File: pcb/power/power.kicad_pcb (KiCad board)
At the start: 2 copper layers, 50 x 40 mm, 98 parts, among them CON1 BARREL_JACK, P1 CONN_01X04, P2 CONN_01X04, P3 CONN_01X04, P4 USB_A, P5 CONN_01X03, P6 CONN_01X03, Q1 MMBT3904, Q2 MMBT3904, Q3 MMBT3904, Q4 MMBT3904, Q5 MMBT3904, Q6 MMBT3904, Q7 DMG2305UX, Q8 DMG2305UX, Q9 DMG2305UX, U1 LM2840, U2 TS30012, U3 LM324QT

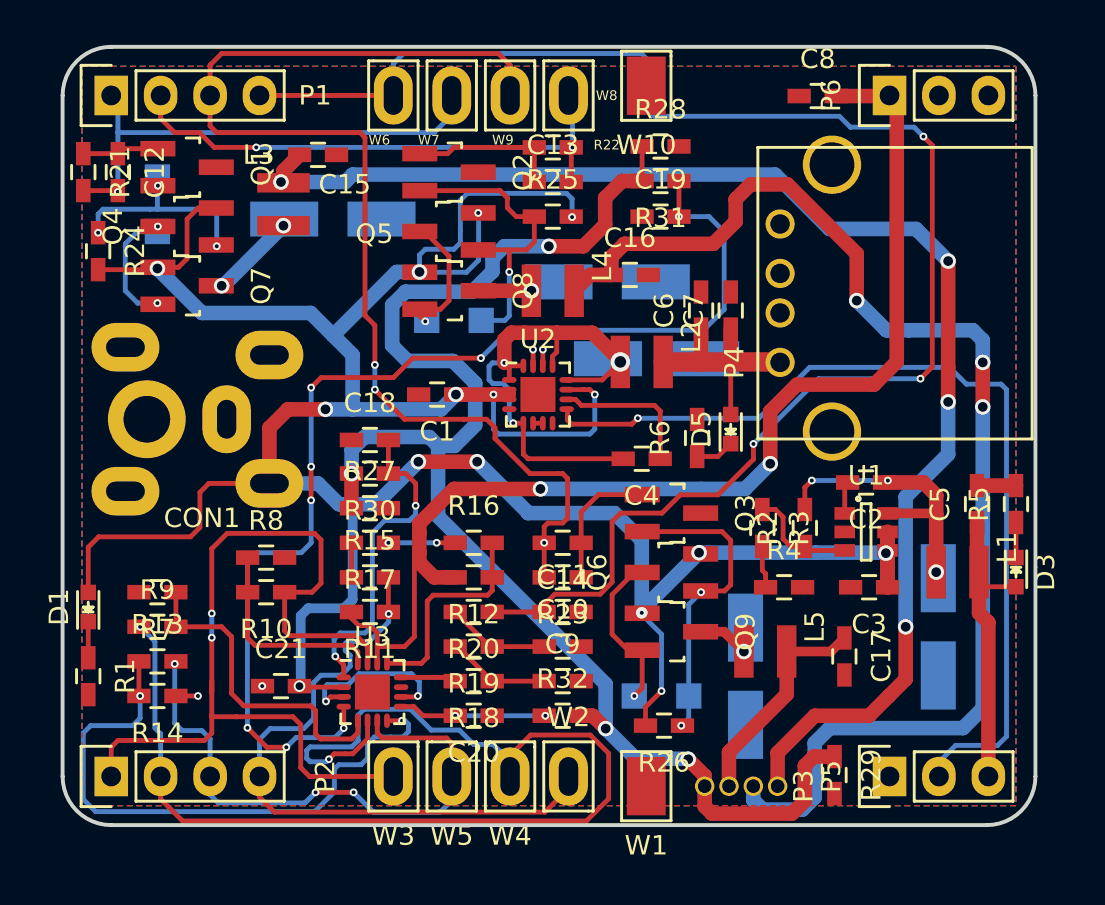
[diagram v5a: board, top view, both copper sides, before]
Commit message: Finished the layout. Could be produced like that. Some fine tuning will maybe be done if I see something, which bothers me.
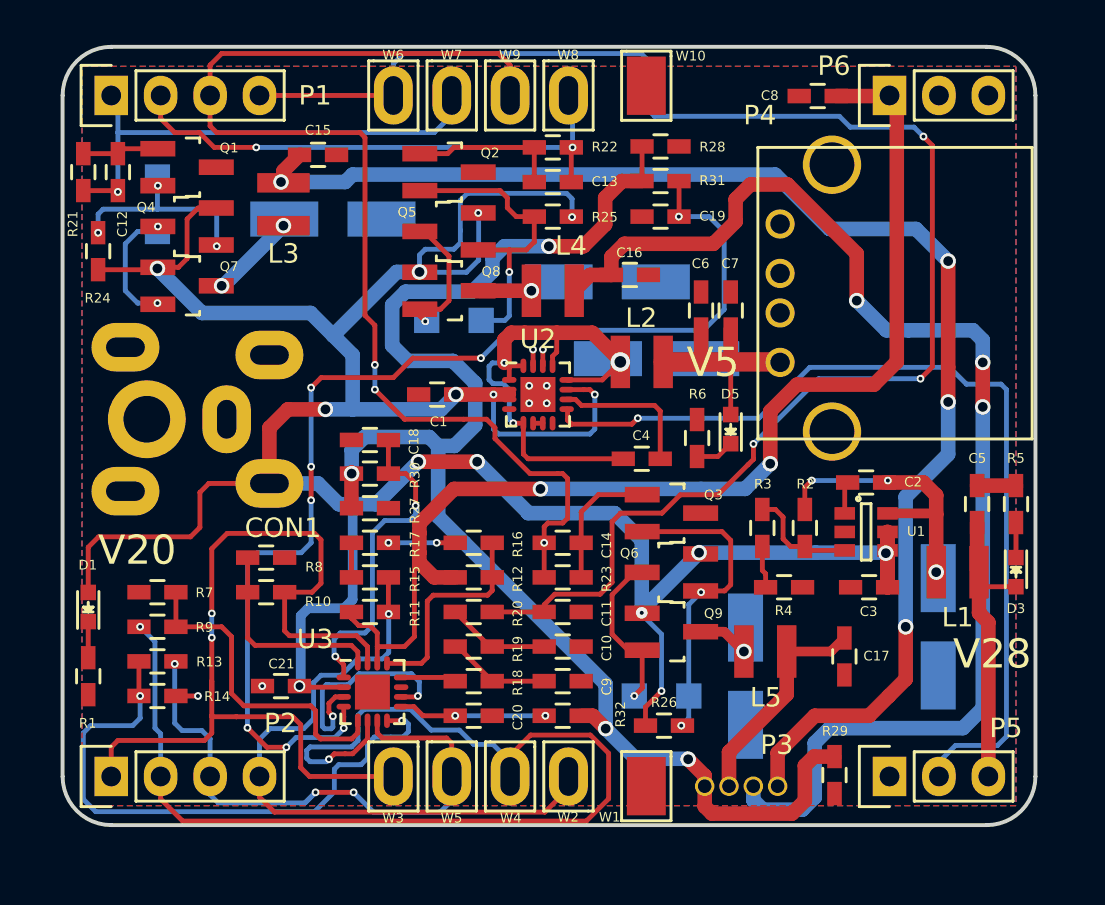
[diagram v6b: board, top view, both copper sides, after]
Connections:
- U2 pad 17: (no net) -> GND
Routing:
- net Net-(U3-Pad10): track 8.74 -> 11.9 mm
- net GND: track 8.54 -> 8.83 mm, vias 6 -> 10
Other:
- board text added: "V20"
- board text added: "V28"
- board text added: "V5"

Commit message: Fnished board. Producing output now.
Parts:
- added G***: LOGO, Additional:UU, B.Cu at (153.9, 110.4)
- added REF**: Via_GND_04, Additional:Via_GND_04, F.Cu at (156.9, 92.8)
- added REF**: Via_GND_04, Additional:Via_GND_04, F.Cu at (153.4, 116.8)
- added REF**: Via_GND_04, Additional:Via_GND_04, F.Cu at (153.4, 115.0)
- added REF**: Via_GND_04, Additional:Via_GND_04, F.Cu at (149.9, 114.9)
- added REF**: Via_GND_04, Additional:Via_GND_04, F.Cu at (153.4, 111.5)
- added REF**: Via_GND_04, Additional:Via_GND_04, F.Cu at (150.9, 90.8)
- added REF**: Via_GND_04, Additional:Via_GND_04, F.Cu at (151.9, 90.8)
- added REF**: Via_GND_04, Additional:Via_GND_04, F.Cu at (146.5, 90.8)
- added REF**: Via_GND_04, Additional:Via_GND_04, F.Cu at (154.5, 105.5)
- added REF**: Via_GND_04, Additional:Via_GND_04, F.Cu at (156.7, 105.5)
- added REF**: Via_GND_04, Additional:Via_GND_04, F.Cu at (158.7, 105.2)
- added REF**: Via_GND_04, Additional:Via_GND_04, F.Cu at (143.2, 116.6)
- added REF**: Via_GND_04, Additional:Via_GND_04, F.Cu at (161.6, 105.2)
- added REF**: Via_GND_04, Additional:Via_GND_04, F.Cu at (144.0, 91.1)
- added REF**: Via_GND_04, Additional:Via_GND_04, F.Cu at (149.6, 111.0)
- added REF**: Via_GND_04, Additional:Via_GND_04, F.Cu at (152.8, 94.3)
- added REF**: Via_GND_1, Additional:Via_GND_1, F.Cu at (140.7, 97.4)
- added REF**: Vian_GND_1, Additional:Via_GND_1, F.Cu at (143.4, 86.5)
- added REF**: Vian_GND_1, Additional:Via_GND_1, F.Cu at (163.3, 102.7)
- added REF**: Vian_GND_1, Additional:Via_GND_1, F.Cu at (177.5, 93.9)
- added REF**: Vian_GND_1, Additional:Via_GND_1, F.Cu at (142.7, 97.4)
- added REF**: Vian_GND_1, Additional:Via_GND_1, F.Cu at (144.0, 96.4)
- added REF**: Via_GND_04, Additional:Via_GND_04, F.Cu at (143.2, 114.7)
- added REF**: Vian_GND_1, Additional:Via_GND_1, F.Cu at (144.0, 94.6)
- added REF**: Vian_GND_1, Additional:Via_GND_1, F.Cu at (177.5, 95.1)
- added REF**: Vian_GND_1, Additional:Via_GND_1, F.Cu at (177.5, 96.4)
- added REF**: Vian_GND_1, Additional:Via_GND_1, F.Cu at (165.1, 97.1)
- added REF**: Vian_GND_1, Additional:Via_GND_1, F.Cu at (162.5, 97.1)
- added REF**: Vian_GND_1, Additional:Via_GND_1, F.Cu at (160.8, 97.1)
- added REF**: Vian_GND_1, Additional:Via_GND_1, F.Cu at (160.8, 98.6)
- added REF**: Vian_GND_1, Additional:Via_GND_1, F.Cu at (166.9, 87.0)
- added REF**: Vian_GND_1, Additional:Via_GND_1, F.Cu at (165.3, 87.0)
- added REF**: Vian_GND_1, Additional:Via_GND_1, F.Cu at (163.8, 87.0)
- added REF**: Via_GND_04, Additional:Via_GND_04, F.Cu at (143.9, 111.4)
- added REF**: Vian_GND_1, Additional:Via_GND_1, F.Cu at (162.3, 87.0)
- added REF**: Vian_GND_1, Additional:Via_GND_1, F.Cu at (158.5, 87.0)
- added REF**: Vian_GND_1, Additional:Via_GND_1, F.Cu at (177.5, 92.6)
- added REF**: Vian_GND_1, Additional:Via_GND_1, F.Cu at (169.2, 112.8)
- added REF**: Vian_GND_1, Additional:Via_GND_1, F.Cu at (171.4, 114.1)
- added REF**: Vian_GND_1, Additional:Via_GND_1, F.Cu at (171.4, 115.6)
- added REF**: Vian_GND_1, Additional:Via_GND_1, F.Cu at (171.4, 117.2)
- added REF**: Vian_GND_1, Additional:Via_GND_1, F.Cu at (170.2, 118.1)
- added REF**: Vian_GND_1, Additional:Via_GND_1, F.Cu at (168.9, 118.1)
- added REF**: Vian_GND_1, Additional:Via_GND_1, F.Cu at (164.1, 118.7)
- added REF**: Via_GND_04, Additional:Via_GND_04, F.Cu at (143.9, 113.0)
- added REF**: Vian_GND_1, Additional:Via_GND_1, F.Cu at (156.3, 118.1)
- added REF**: Vian_GND_1, Additional:Via_GND_1, F.Cu at (151.7, 109.1)
- added REF**: Vian_GND_1, Additional:Via_GND_1, F.Cu at (147.0, 110.9)
- added REF**: Vian_GND_1, Additional:Via_GND_1, F.Cu at (141.4, 111.9)
- added REF**: Vian_GND_1, Additional:Via_GND_1, F.Cu at (140.4, 114.5)
- added REF**: Vian_GND_1, Additional:Via_GND_1, F.Cu at (140.4, 116.7)
- added REF**: Vian_GND_1, Additional:Via_GND_1, F.Cu at (138.7, 120.6)
- added REF**: Vian_GND_1, Additional:Via_GND_1, F.Cu at (136.7, 118.4)
- added REF**: Vian_GND_1, Additional:Via_GND_1, F.Cu at (136.6, 111.9)
- added REF**: Vian_GND_1, Additional:Via_GND_1, F.Cu at (138.2, 108.8)
- added REF**: Via_GND_04, Additional:Via_GND_04, F.Cu at (153.3, 118.5)
- added REF**: Vian_GND_1, Additional:Via_GND_1, F.Cu at (132.5, 111.9)
- added REF**: Vian_GND_1, Additional:Via_GND_1, F.Cu at (132.4, 115.7)
- added REF**: Vian_GND_1, Additional:Via_GND_1, F.Cu at (132.5, 119.0)
- added REF**: Vian_GND_1, Additional:Via_GND_1, F.Cu at (143.5, 88.5)
- added REF**: Vian_GND_1, Additional:Via_GND_1, F.Cu at (146.5, 94.6)
- added REF**: Via_GND_04, Additional:Via_GND_04, F.Cu at (151.1, 118.5)
- added REF**: Via_GND_04, Additional:Via_GND_04, F.Cu at (150.1, 118.5)
- added REF**: Via_GND_04, Additional:Via_GND_04, F.Cu at (149.9, 116.7)
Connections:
- U3 pad 17: (no net) -> GND
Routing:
- net GND: track 8.83 -> 6.92 mm, vias 10 -> 20
- net ADC_B: track 62.9 -> 62.3 mm
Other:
- rule trace_min: 0.2 -> 0.1
- board text added: "Max & Elmar December 2016"
- board text added: "Swakeup Power Board v1.0"

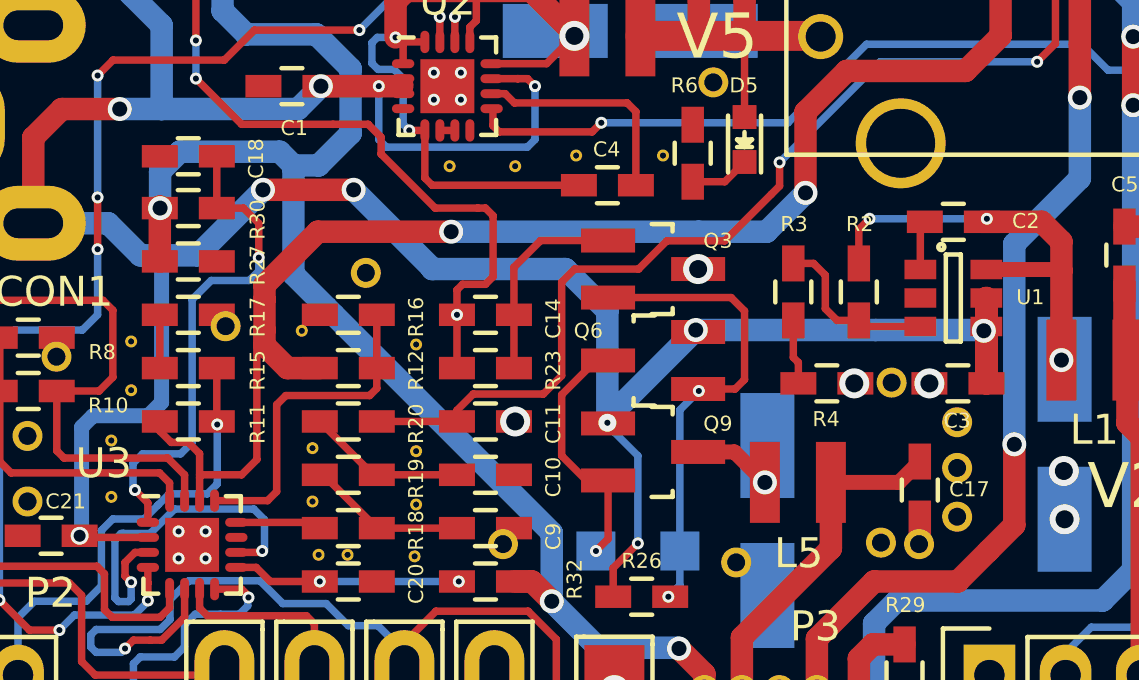
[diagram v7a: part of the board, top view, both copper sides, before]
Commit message: Added some stitching vias.
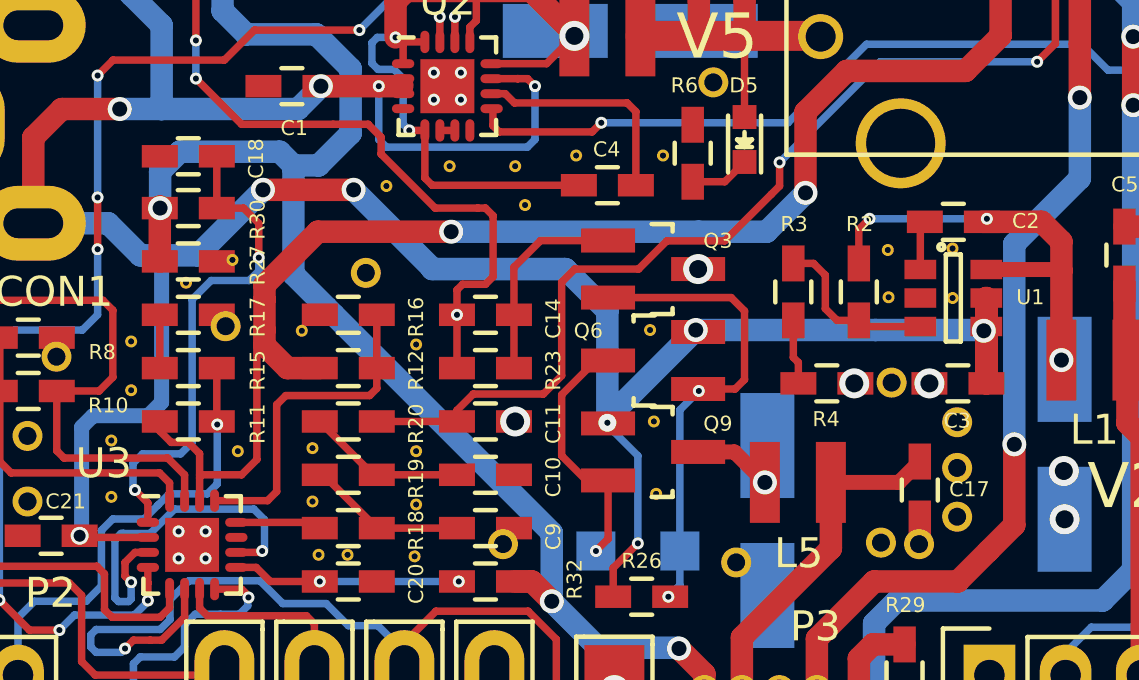
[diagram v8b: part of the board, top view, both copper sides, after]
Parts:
- added G***: LOGO, Additional:UU, B.Cu at (152.1, 112.0)
- added REF**: Via_GND_04, Additional:Via_GND_04, F.Cu at (171.3, 108.3)
- added REF**: Via_GND_04, Additional:Via_GND_04, F.Cu at (171.3, 109.9)
- added REF**: Via_GND_04, Additional:Via_GND_04, F.Cu at (169.1, 108.3)
- added REF**: Via_GND_04, Additional:Via_GND_04, F.Cu at (152.4, 106.2)
- added REF**: Via_GND_04, Additional:Via_GND_04, F.Cu at (147.3, 108.7)
- added REF**: Via_GND_04, Additional:Via_GND_04, F.Cu at (145.7, 109.4)
- added REF**: Via_GND_04, Additional:Via_GND_04, F.Cu at (147.4, 115.0)
- added REF**: Via_GND_04, Additional:Via_GND_04, F.Cu at (161.3, 114.0)
- added REF**: Via_GND_04, Additional:Via_GND_04, F.Cu at (161.4, 116.5)
- added REF**: Via_GND_04, Additional:Via_GND_04, F.Cu at (161.2, 111.0)
- added REF**: Via_GND_04, Additional:Via_GND_04, F.Cu at (169.1, 109.9)
- added REF**: Via_GND_04, Additional:Via_GND_04, F.Cu at (157.0, 106.8)
